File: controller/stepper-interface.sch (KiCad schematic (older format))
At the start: 0 parts

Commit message: More or less final controller board
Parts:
- added J6: CONN_01X05, symbol CONN_01X05
- added Q9: Q_NMOS_GSD, Housings_SOT-23_SOT-143_TSOT-6:SOT-23_Handsoldering, symbol Q_NMOS_GSD
- added R63: 169R, Resistors_SMD:R_0603_HandSoldering, symbol R
- added R64: 100k, Resistors_SMD:R_0603_HandSoldering, symbol R
- added R65, R66, R67: 330, Resistors_SMD:R_0603_HandSoldering, symbol R
- added R68: 1k, Resistors_SMD:R_0603_HandSoldering, symbol R
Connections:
- new net: Q9.1 (G), R63.1, R64.1
- new net +5V: R67.1, R68.1
- new net GECKO_DIR: J6.2 (P2), R65.1
- new net GECKO_DISABLE: J6.1 (P1), Q9.3 (D), R67.2
- new net GECKO_STEP: J6.3 (P3), R66.1
- new net GND: J6.4 (P4), Q9.2 (S), R64.2
- new net STEERING_DIR: R65.2
- new net STEERING_ENABLE: R63.2
- new net STEERING_FAULT: J6.5 (P5), R68.2
- new net STEERING_STEP: R66.2
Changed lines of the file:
@@
 LIBS:valves
 LIBS:mic-parts
+LIBS:shield_arduino
 LIBS:controller-cache
 EELAYER 26 0
@@
 $Descr A4 11693 8268
 encoding utf-8
-Sheet 1 10
+Sheet 7 10
 Title ""
 Date ""
@@
 Comment4 ""
 $EndDescr
+$Comp
+L CONN_01X05 J6
+U 1 1 58CA4536
+P 9200 3350
+F 0 "J6" H 9278 3391 50  0000 L CNN
+F 1 "CONN_01X05" H 9278 3300 50  0000 L CNN
+F 2 "" H 9200 3350 50  0001 C CNN
+F 3 "" H 9200 3350 50  0001 C CNN
+	1    9200 3350
+	1    0    0    -1
+$EndComp
+Wire Wire Line
+	6650 3150 9000 3150
+Wire Wire Line
+	9000 3250 7750 3250
+Wire Wire Line
+	9000 3350 7750 3350
+Wire Wire Line
+	7050 3450 9000 3450
+Wire Wire Line
+	5400 3550 9000 3550
+Text Label 7750 3150 0    60   ~ 0
+GECKO_DISABLE
+Text Label 7750 3250 0    60   ~ 0
+GECKO_DIR
+Text Label 7750 3350 0    60   ~ 0
+GECKO_STEP
+Text Label 7750 3450 0    60   ~ 0
+GECKO_COMMON_GND
+Text Label 7750 3550 0    60   ~ 0
+GECKO_FAULT
+Text HLabel 7200 2350 0    60   Input ~ 0
++5V
+$Comp
+L R R67
+U 1 1 58CA49EF
+P 8550 2850
+F 0 "R67" H 8619 2896 50  0000 L CNN
+F 1 "330" H 8619 2805 50  0000 L CNN
+F 2 "Resistors_SMD:R_0603_HandSoldering" V 4080 -50 50  0001 C CNN
+F 3 "" H 4150 -50 50  0001 C CNN
+F 4 "?" H 8550 2850 60  0001 C CNN "PartNo"
+F 5 "?" H 8550 2850 60  0001 C CNN "Manufacturer"
+F 6 "?" H 8550 2850 60  0001 C CNN "Distributor"
+	1    8550 2850
+	-1   0    0    -1
+$EndComp
+Wire Wire Line
+	7200 2350 8900 2350
+Wire Wire Line
+	8550 2350 8550 2700
+Wire Wire Line
+	8550 3000 8550 3150
+Connection ~ 8550 3150
+$Comp
+L Q_NMOS_GSD Q9
+U 1 1 58CA4F34
+P 6550 3800
+F 0 "Q9" H 6756 3800 50  0000 L CNN
+F 1 "Q_NMOS_GSD" H 6755 3755 50  0001 L CNN
+F 2 "Housings_SOT-23_SOT-143_TSOT-6:SOT-23_Handsoldering" H 2750 1200 50  0001 C CNN
+F 3 "" H 2550 1100 50  0001 C CNN
+	1    6550 3800
+	1    0    0    -1
+$EndComp
+Wire Wire Line
+	6650 3150 6650 3600
+$Comp
+L GND #PWR014
+U 1 1 58CA4F91
+P 6650 4100
+F 0 "#PWR014" H 6650 3850 50  0001 C CNN
+F 1 "GND" H 6655 3927 50  0000 C CNN
+F 2 "" H 6650 4100 50  0001 C CNN
+F 3 "" H 6650 4100 50  0001 C CNN
+	1    6650 4100
+	1    0    0    -1
+$EndComp
+$Comp
+L GND #PWR015
+U 1 1 58CA4FA9
+P 7050 4000
+F 0 "#PWR015" H 7050 3750 50  0001 C CNN
+F 1 "GND" H 7055 3827 50  0000 C CNN
+F 2 "" H 7050 4000 50  0001 C CNN
+F 3 "" H 7050 4000 50  0001 C CNN
+	1    7050 4000
+	1    0    0    -1
+$EndComp
+Wire Wire Line
+	7050 3450 7050 4000
+$Comp
+L R R64
+U 1 1 58CA4FE1
+P 6350 3950
+F 0 "R64" V 6557 3950 50  0000 C CNN
+F 1 "100k" V 6466 3950 50  0000 C CNN
+F 2 "Resistors_SMD:R_0603_HandSoldering" V 1880 1050 50  0001 C CNN
+F 3 "" H 1950 1050 50  0001 C CNN
+F 4 "?" H 6350 3950 60  0001 C CNN "PartNo"
+F 5 "?" H 6350 3950 60  0001 C CNN "Manufacturer"
+F 6 "?" H 6350 3950 60  0001 C CNN "Distributor"
+	1    6350 3950
+	-1   0    0    -1
+$EndComp
+$Comp
+L R R63
+U 1 1 58CA5047
+P 6200 3800
+F 0 "R63" V 6407 3800 50  0000 C CNN
+F 1 "169R" V 6316 3800 50  0000 C CNN
+F 2 "Resistors_SMD:R_0603_HandSoldering" V 1730 900 50  0001 C CNN
+F 3 "" H 1800 900 50  0001 C CNN
+F 4 "?" H 6200 3800 60  0001 C CNN "PartNo"
+F 5 "?" H 6200 3800 60  0001 C CNN "Manufacturer"
+F 6 "?" H 6200 3800 60  0001 C CNN "Distributor"
+	1    6200 3800
+	0    1    -1   0
+$EndComp
+Connection ~ 6350 3800
+Wire Wire Line
+	6650 4000 6650 4100
+Wire Wire Line
+	6650 4100 6350 4100
+Connection ~ 6650 4100
+Wire Wire Line
+	6050 3800 5400 3800
+Text HLabel 5400 3800 0    60   Input ~ 0
+STEERING_ENABLE
+$Comp
+L R R65
+U 1 1 58CA511C
+P 7600 3250
+F 0 "R65" V 7807 3250 50  0000 C CNN
+F 1 "330" V 7716 3250 50  0000 C CNN
+F 2 "Resistors_SMD:R_0603_HandSoldering" V 3130 350 50  0001 C CNN
+F 3 "" H 3200 350 50  0001 C CNN
+F 4 "?" H 7600 3250 60  0001 C CNN "PartNo"
+F 5 "?" H 7600 3250 60  0001 C CNN "Manufacturer"
+F 6 "?" H 7600 3250 60  0001 C CNN "Distributor"
+	1    7600 3250
+	0    1    -1   0
+$EndComp
+$Comp
+L R R66
+U 1 1 58CA51EA
+P 7600 3350
+F 0 "R66" V 7807 3350 50  0000 C CNN
+F 1 "330" V 7716 3350 50  0000 C CNN
+F 2 "Resistors_SMD:R_0603_HandSoldering" V 3130 450 50  0001 C CNN
+F 3 "" H 3200 450 50  0001 C CNN
+F 4 "?" H 7600 3350 60  0001 C CNN "PartNo"
+F 5 "?" H 7600 3350 60  0001 C CNN "Manufacturer"
+F 6 "?" H 7600 3350 60  0001 C CNN "Distributor"
+	1    7600 3350
+	0    1    -1   0
+$EndComp
+Wire Wire Line
+	7450 3250 5400 3250
+Wire Wire Line
+	7450 3350 5400 3350
+Text HLabel 5400 3350 0    60   Input ~ 0
+STEERING_STEP
+Text HLabel 5400 3250 0    60   Input ~ 0
+STEERING_DIR
+$Comp
+L R R68
+U 1 1 58CA539C
+P 8900 2850
+F 0 "R68" H 8969 2896 50  0000 L CNN
+F 1 "1k" H 8969 2805 50  0000 L CNN
+F 2 "Resistors_SMD:R_0603_HandSoldering" V 4430 -50 50  0001 C CNN
+F 3 "" H 4500 -50 50  0001 C CNN
+F 4 "?" H 8900 2850 60  0001 C CNN "PartNo"
+F 5 "?" H 8900 2850 60  0001 C CNN "Manufacturer"
+F 6 "?" H 8900 2850 60  0001 C CNN "Distributor"
+	1    8900 2850
+	-1   0    0    -1
+$EndComp
+Wire Wire Line
+	8900 3000 8900 3550
+Connection ~ 8900 3550
+Wire Wire Line
+	8900 2350 8900 2700
+Connection ~ 8550 2350
+Text HLabel 5400 3550 0    60   Input ~ 0
+STEERING_FAULT
 $EndSCHEMATC

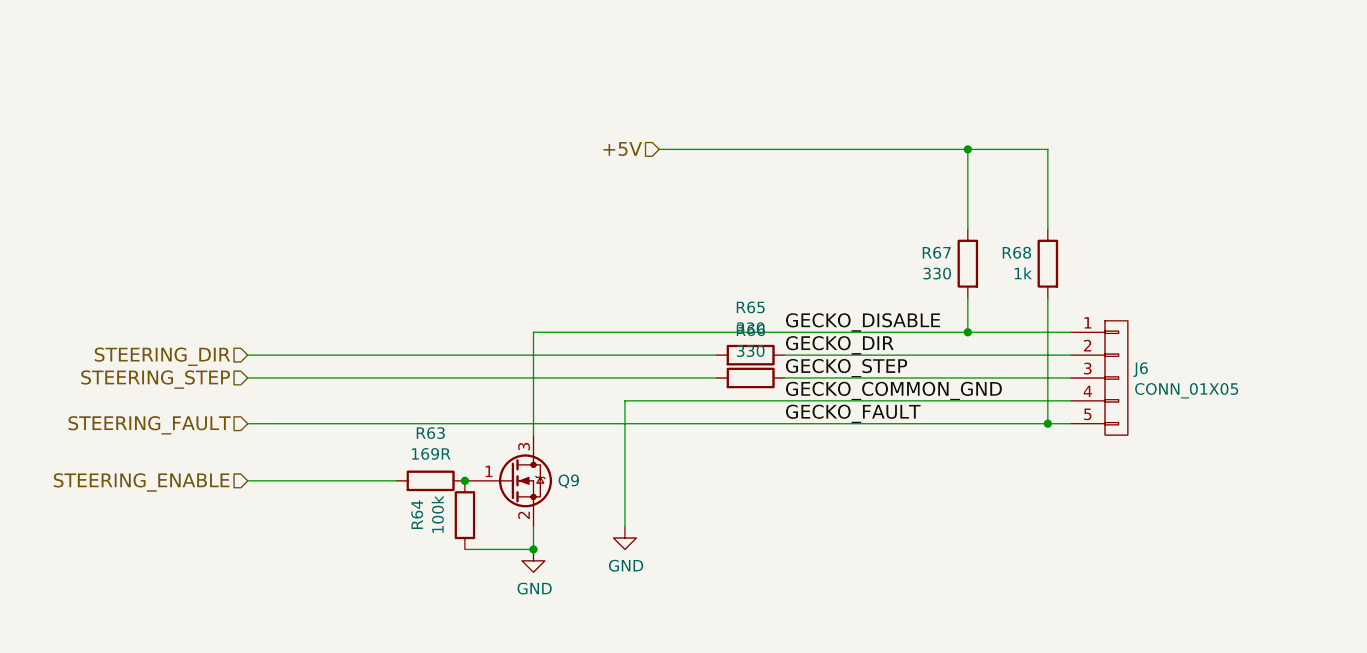
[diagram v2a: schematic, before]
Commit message: Finish the routing, add some significant fixes: *correct to-252 pin numbering * longer pads for relays * fix footprint of the optocouplers
Also finish the routing
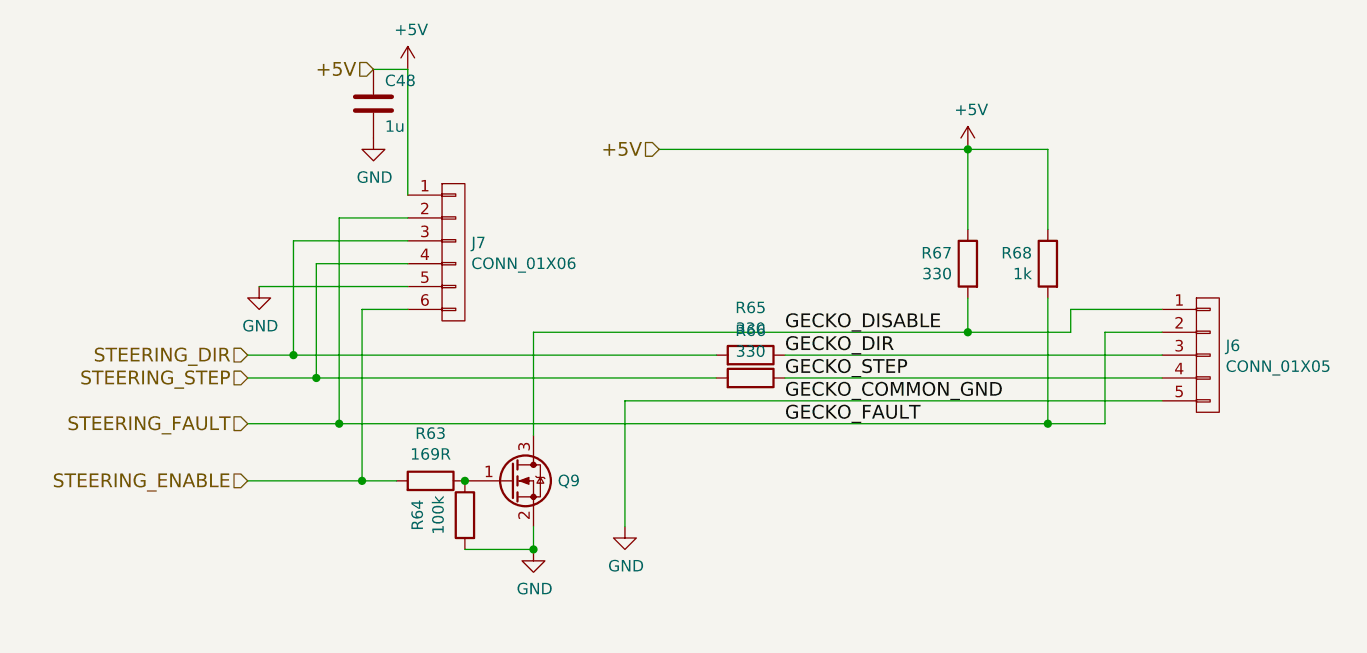
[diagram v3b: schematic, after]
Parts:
- added C48: 1u, Capacitors_SMD:C_0603, symbol C
- added J7: CONN_01X06, Socket_Strips:Socket_Strip_Straight_1x06_Pitch2.54mm, symbol CONN_01X06
- J6: footprint (none) -> Connectors_Terminal_Blocks:TerminalBlock_Pheonix_MKDS1.5-5pol; Distributor (none) -> ?; Manufacturer (none) -> ?; PartNo (none) -> ?
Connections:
- net +5V: now also C48.1, J7.1 (P1)
- net GECKO_DIR: now also J6.3 (P3); no longer J6.2 (P2)
- net GECKO_STEP: now also J6.4 (P4); no longer J6.3 (P3)
- net GND: now also J6.5 (P5), C48.2, J7.5 (P5); no longer J6.4 (P4)
- net STEERING_DIR: now also J7.3 (P3)
- net STEERING_ENABLE: now also J7.6 (P6)
- net STEERING_FAULT: now also J6.2 (P2), J7.2 (P2); no longer J6.5 (P5)
- net STEERING_STEP: now also J7.4 (P4)
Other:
- moved on the sheet: J6
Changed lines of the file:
@@
 L CONN_01X05 J6
 U 1 1 58CA4536
-P 9200 3350
-F 0 "J6" H 9278 3391 50  0000 L CNN
-F 1 "CONN_01X05" H 9278 3300 50  0000 L CNN
-F 2 "" H 9200 3350 50  0001 C CNN
-F 3 "" H 9200 3350 50  0001 C CNN
-	1    9200 3350
+P 9600 3250
+F 0 "J6" H 9678 3291 50  0000 L CNN
+F 1 "CONN_01X05" H 9678 3200 50  0000 L CNN
+F 2 "Connectors_Terminal_Blocks:TerminalBlock_Pheonix_MKDS1.5-5pol" H 9600 3250 50  0001 C CNN
+F 3 "" H 9600 3250 50  0001 C CNN
+F 4 "?" H 9600 3250 60  0001 C CNN "PartNo"
+F 5 "?" H 9600 3250 60  0001 C CNN "Manufacturer"
+F 6 "?" H 9600 3250 60  0001 C CNN "Distributor"
+	1    9600 3250
 	1    0    0    -1
 $EndComp
@@
 	6650 3150 9000 3150
 Wire Wire Line
-	9000 3250 7750 3250
-Wire Wire Line
-	9000 3350 7750 3350
-Wire Wire Line
-	7050 3450 9000 3450
-Wire Wire Line
-	5400 3550 9000 3550
+	7750 3250 9400 3250
+Wire Wire Line
+	7750 3350 9400 3350
+Wire Wire Line
+	7050 3450 9400 3450
+Wire Wire Line
+	5400 3550 9150 3550
 Text Label 7750 3150 0    60   ~ 0
 GECKO_DISABLE
@@
 Text HLabel 5400 3550 0    60   Input ~ 0
 STEERING_FAULT
+Wire Wire Line
+	6100 3050 5900 3050
+Wire Wire Line
+	5900 3050 5900 3800
+Connection ~ 5900 3800
+Connection ~ 5800 3550
+Wire Wire Line
+	5700 3350 5700 2850
+Wire Wire Line
+	5700 2850 6100 2850
+Connection ~ 5700 3350
+Wire Wire Line
+	5600 3250 5600 2750
+Wire Wire Line
+	5600 2750 6100 2750
+Connection ~ 5600 3250
+$Comp
+L CONN_01X06 J7
+U 1 1 58CF2456
+P 6300 2800
+F 0 "J7" H 6378 2841 50  0000 L CNN
+F 1 "CONN_01X06" H 6378 2750 50  0000 L CNN
+F 2 "Socket_Strips:Socket_Strip_Straight_1x06_Pitch2.54mm" H 6300 2800 50  0001 C CNN
+F 3 "" H 6300 2800 50  0001 C CNN
+F 4 "?" H 6300 2800 60  0001 C CNN "PartNo"
+F 5 "?" H 6300 2800 60  0001 C CNN "Manufacturer"
+F 6 "?" H 6300 2800 60  0001 C CNN "Distributor"
+	1    6300 2800
+	1    0    0    -1
+$EndComp
+Text HLabel 5950 2000 0    60   Input ~ 0
++5V
+$Comp
+L GND #PWR018
+U 1 1 58CF24DE
+P 5450 2950
+F 0 "#PWR018" H 5450 2700 50  0001 C CNN
+F 1 "GND" H 5455 2777 50  0000 C CNN
+F 2 "" H 5450 2950 50  0001 C CNN
+F 3 "" H 5450 2950 50  0001 C CNN
+	1    5450 2950
+	1    0    0    -1
+$EndComp
+Wire Wire Line
+	6100 2950 5450 2950
+Wire Wire Line
+	5800 3550 5800 2650
+Wire Wire Line
+	5800 2650 6100 2650
+Wire Wire Line
+	9000 3150 9000 3050
+Wire Wire Line
+	9000 3050 9400 3050
+Wire Wire Line
+	9150 3550 9150 3150
+Wire Wire Line
+	9150 3150 9400 3150
+$Comp
+L C C48
+U 1 1 58CF2F69
+P 5950 2150
+F 0 "C48" H 6000 2250 50  0000 L CNN
+F 1 "1u" H 6000 2050 50  0000 L CNN
+F 2 "Capacitors_SMD:C_0603" H 5988 2000 30  0001 C CNN
+F 3 "" H 5950 2150 60  0000 C CNN
+	1    5950 2150
+	1    0    0    -1
+$EndComp
+$Comp
+L GND #PWR019
+U 1 1 58CF2F7A
+P 5950 2300
+F 0 "#PWR019" H 5950 2050 50  0001 C CNN
+F 1 "GND" H 5955 2127 50  0000 C CNN
+F 2 "" H 5950 2300 50  0001 C CNN
+F 3 "" H 5950 2300 50  0001 C CNN
+	1    5950 2300
+	1    0    0    -1
+$EndComp
+Wire Wire Line
+	5950 2000 6100 2000
+Wire Wire Line
+	6100 2000 6100 2550
+$Comp
+L +5V #PWR020
+U 1 1 58CF31AE
+P 6100 2000
+F 0 "#PWR020" H 6100 1850 50  0001 C CNN
+F 1 "+5V" H 6115 2173 50  0000 C CNN
+F 2 "" H 6100 2000 50  0001 C CNN
+F 3 "" H 6100 2000 50  0001 C CNN
+	1    6100 2000
+	1    0    0    -1
+$EndComp
+$Comp
+L +5V #PWR021
+U 1 1 58CF31E8
+P 8550 2350
+F 0 "#PWR021" H 8550 2200 50  0001 C CNN
+F 1 "+5V" H 8565 2523 50  0000 C CNN
+F 2 "" H 8550 2350 50  0001 C CNN
+F 3 "" H 8550 2350 50  0001 C CNN
+	1    8550 2350
+	1    0    0    -1
+$EndComp
 $EndSCHEMATC

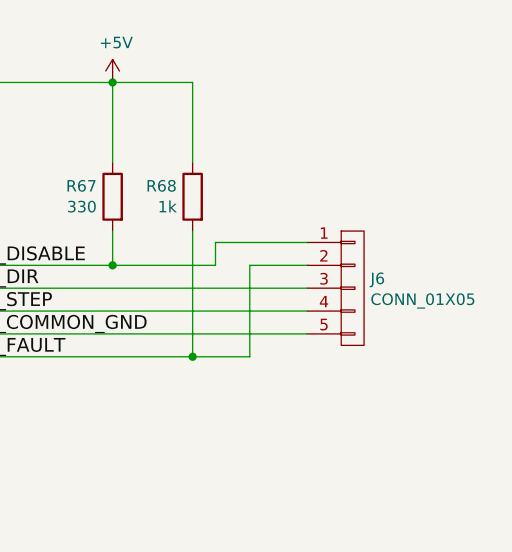
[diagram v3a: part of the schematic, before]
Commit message: Update the 5 and 2 pin terminal footprints, shuffle around some tracks
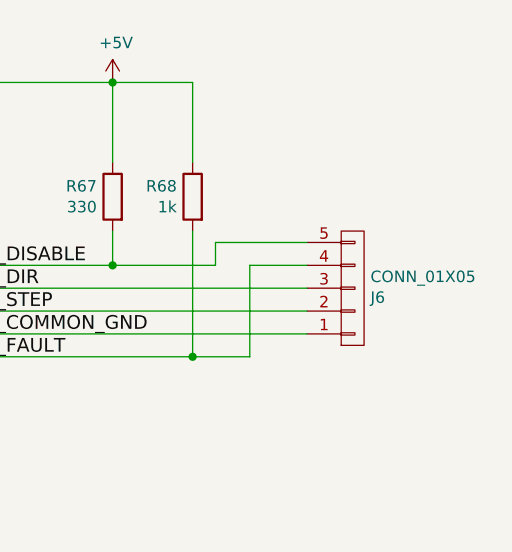
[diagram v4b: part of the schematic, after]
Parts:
- J6: footprint Connectors_Terminal_Blocks:TerminalBlock_Pheonix_MKDS1.5-5pol -> smalsiukas-footpints:TerminalBlock_5.08-5pol
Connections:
- net GECKO_DISABLE: now also J6.5 (P5); no longer J6.1 (P1)
- net GECKO_STEP: now also J6.2 (P2); no longer J6.4 (P4)
- net GND: now also J6.1 (P1); no longer J6.5 (P5)
- net STEERING_FAULT: now also J6.4 (P4); no longer J6.2 (P2)
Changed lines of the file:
@@
 F 0 "J6" H 9678 3291 50  0000 L CNN
 F 1 "CONN_01X05" H 9678 3200 50  0000 L CNN
-F 2 "Connectors_Terminal_Blocks:TerminalBlock_Pheonix_MKDS1.5-5pol" H 9600 3250 50  0001 C CNN
+F 2 "smalsiukas-footpints:TerminalBlock_5.08-5pol" H 9600 3250 50  0001 C CNN
 F 3 "" H 9600 3250 50  0001 C CNN
 F 4 "?" H 9600 3250 60  0001 C CNN "PartNo"
@@
 F 6 "?" H 9600 3250 60  0001 C CNN "Distributor"
 	1    9600 3250
-	1    0    0    -1
+	1    0    0    1
 $EndComp
 Wire Wire Line

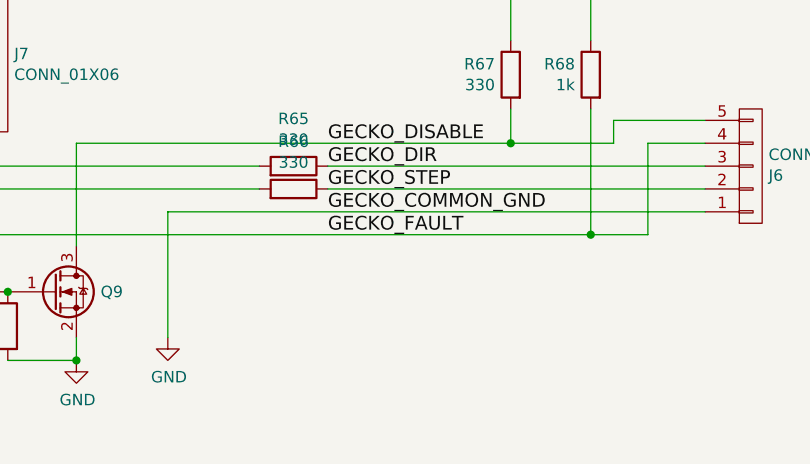
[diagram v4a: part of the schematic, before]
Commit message: send controller and line interface boards for manufacturing
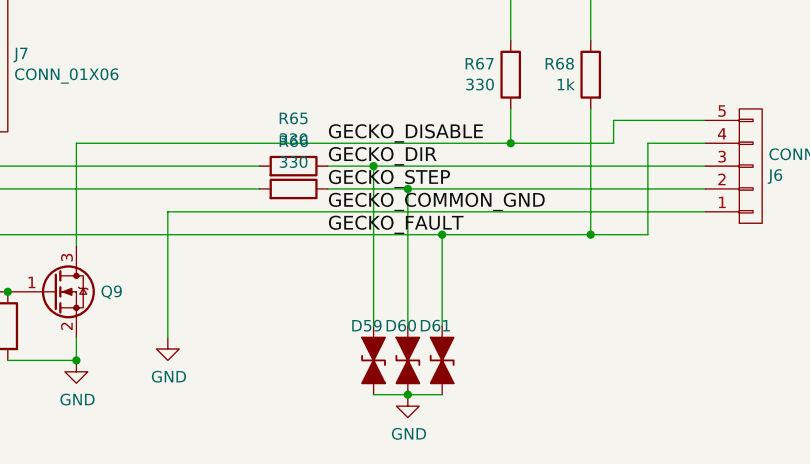
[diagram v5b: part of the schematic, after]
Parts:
- added D59, D60, D61: D_TVS_ALT, Diodes_SMD:SOD-323, symbol D_TVS_ALT
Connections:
- net GECKO_DIR: now also D59.1 (A1)
- net GECKO_STEP: now also D60.1 (A1)
- net GND: now also D59.2 (A2), D60.2 (A2), D61.2 (A2)
- net STEERING_FAULT: now also D61.1 (A1)
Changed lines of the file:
@@
 	6650 3150 6650 3600
 $Comp
-L GND #PWR016
+L GND #PWR22
 U 1 1 58CA4F91
 P 6650 4100
-F 0 "#PWR016" H 6650 3850 50  0001 C CNN
+F 0 "#PWR22" H 6650 3850 50  0001 C CNN
 F 1 "GND" H 6655 3927 50  0000 C CNN
 F 2 "" H 6650 4100 50  0001 C CNN
@@
 $EndComp
 $Comp
-L GND #PWR017
+L GND #PWR23
 U 1 1 58CA4FA9
 P 7050 4000
-F 0 "#PWR017" H 7050 3750 50  0001 C CNN
+F 0 "#PWR23" H 7050 3750 50  0001 C CNN
 F 1 "GND" H 7055 3827 50  0000 C CNN
 F 2 "" H 7050 4000 50  0001 C CNN
@@
 +5V
 $Comp
-L GND #PWR018
+L GND #PWR19
 U 1 1 58CF24DE
 P 5450 2950
-F 0 "#PWR018" H 5450 2700 50  0001 C CNN
+F 0 "#PWR19" H 5450 2700 50  0001 C CNN
 F 1 "GND" H 5455 2777 50  0000 C CNN
 F 2 "" H 5450 2950 50  0001 C CNN
@@
 $EndComp
 $Comp
-L GND #PWR019
+L GND #PWR20
 U 1 1 58CF2F7A
 P 5950 2300
-F 0 "#PWR019" H 5950 2050 50  0001 C CNN
+F 0 "#PWR20" H 5950 2050 50  0001 C CNN
 F 1 "GND" H 5955 2127 50  0000 C CNN
 F 2 "" H 5950 2300 50  0001 C CNN
@@
 	6100 2000 6100 2550
 $Comp
-L +5V #PWR020
+L +5V #PWR21
 U 1 1 58CF31AE
 P 6100 2000
-F 0 "#PWR020" H 6100 1850 50  0001 C CNN
+F 0 "#PWR21" H 6100 1850 50  0001 C CNN
 F 1 "+5V" H 6115 2173 50  0000 C CNN
 F 2 "" H 6100 2000 50  0001 C CNN
@@
 $EndComp
 $Comp
-L +5V #PWR021
+L +5V #PWR25
 U 1 1 58CF31E8
 P 8550 2350
-F 0 "#PWR021" H 8550 2200 50  0001 C CNN
+F 0 "#PWR25" H 8550 2200 50  0001 C CNN
 F 1 "+5V" H 8565 2523 50  0000 C CNN
 F 2 "" H 8550 2350 50  0001 C CNN
@@
 	1    0    0    -1
 $EndComp
+$Comp
+L D_TVS_ALT D59
+U 1 1 58D0B63C
+P 7950 4100
+F 0 "D59" V 7800 4000 50  0000 L CNN
+F 1 "D_TVS_ALT" V 7995 4179 50  0001 L CNN
+F 2 "Diodes_SMD:SOD-323" H 7950 4100 50  0001 C CNN
+F 3 "" H 7950 4100 50  0001 C CNN
+F 4 "?" H 7950 4100 60  0001 C CNN "PartNo"
+F 5 "?" H 7950 4100 60  0001 C CNN "Manufacturer"
+F 6 "2059012" H 7950 4100 60  0001 C CNN "Distributor"
+	1    7950 4100
+	0    1    1    0
+$EndComp
+Wire Wire Line
+	7950 3950 7950 3250
+Connection ~ 7950 3250
+$Comp
+L D_TVS_ALT D60
+U 1 1 58D0B852
+P 8100 4100
+F 0 "D60" V 7950 4000 50  0000 L CNN
+F 1 "D_TVS_ALT" V 8145 4179 50  0001 L CNN
+F 2 "Diodes_SMD:SOD-323" H 8100 4100 50  0001 C CNN
+F 3 "" H 8100 4100 50  0001 C CNN
+F 4 "?" H 8100 4100 60  0001 C CNN "PartNo"
+F 5 "?" H 8100 4100 60  0001 C CNN "Manufacturer"
+F 6 "2059012" H 8100 4100 60  0001 C CNN "Distributor"
+	1    8100 4100
+	0    1    1    0
+$EndComp
+Wire Wire Line
+	8100 3950 8100 3350
+Connection ~ 8100 3350
+$Comp
+L D_TVS_ALT D61
+U 1 1 58D0B8BC
+P 8250 4100
+F 0 "D61" V 8100 4000 50  0000 L CNN
+F 1 "D_TVS_ALT" V 8295 4179 50  0001 L CNN
+F 2 "Diodes_SMD:SOD-323" H 8250 4100 50  0001 C CNN
+F 3 "" H 8250 4100 50  0001 C CNN
+F 4 "?" H 8250 4100 60  0001 C CNN "PartNo"
+F 5 "?" H 8250 4100 60  0001 C CNN "Manufacturer"
+F 6 "2059012" H 8250 4100 60  0001 C CNN "Distributor"
+	1    8250 4100
+	0    1    1    0
+$EndComp
+Wire Wire Line
+	8250 3950 8250 3550
+Connection ~ 8250 3550
+Wire Wire Line
+	7950 4250 8250 4250
+Connection ~ 8100 4250
+$Comp
+L GND #PWR24
+U 1 1 58D0B9A6
+P 8100 4250
+F 0 "#PWR24" H 8100 4000 50  0001 C CNN
+F 1 "GND" H 8105 4077 50  0000 C CNN
+F 2 "" H 8100 4250 50  0001 C CNN
+F 3 "" H 8100 4250 50  0001 C CNN
+	1    8100 4250
+	1    0    0    -1
+$EndComp
